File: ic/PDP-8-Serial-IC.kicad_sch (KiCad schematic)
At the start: 61 parts, among them J1 Screw_Terminal_01x06, J2 DE9_Socket_MountingHoles, J3 FlipChip_01x18, Q1 2N3904, Q2 2N3904, Q3 2N3906, U1 MAX232, U2 74HCT14, U3 L78L05_TO92

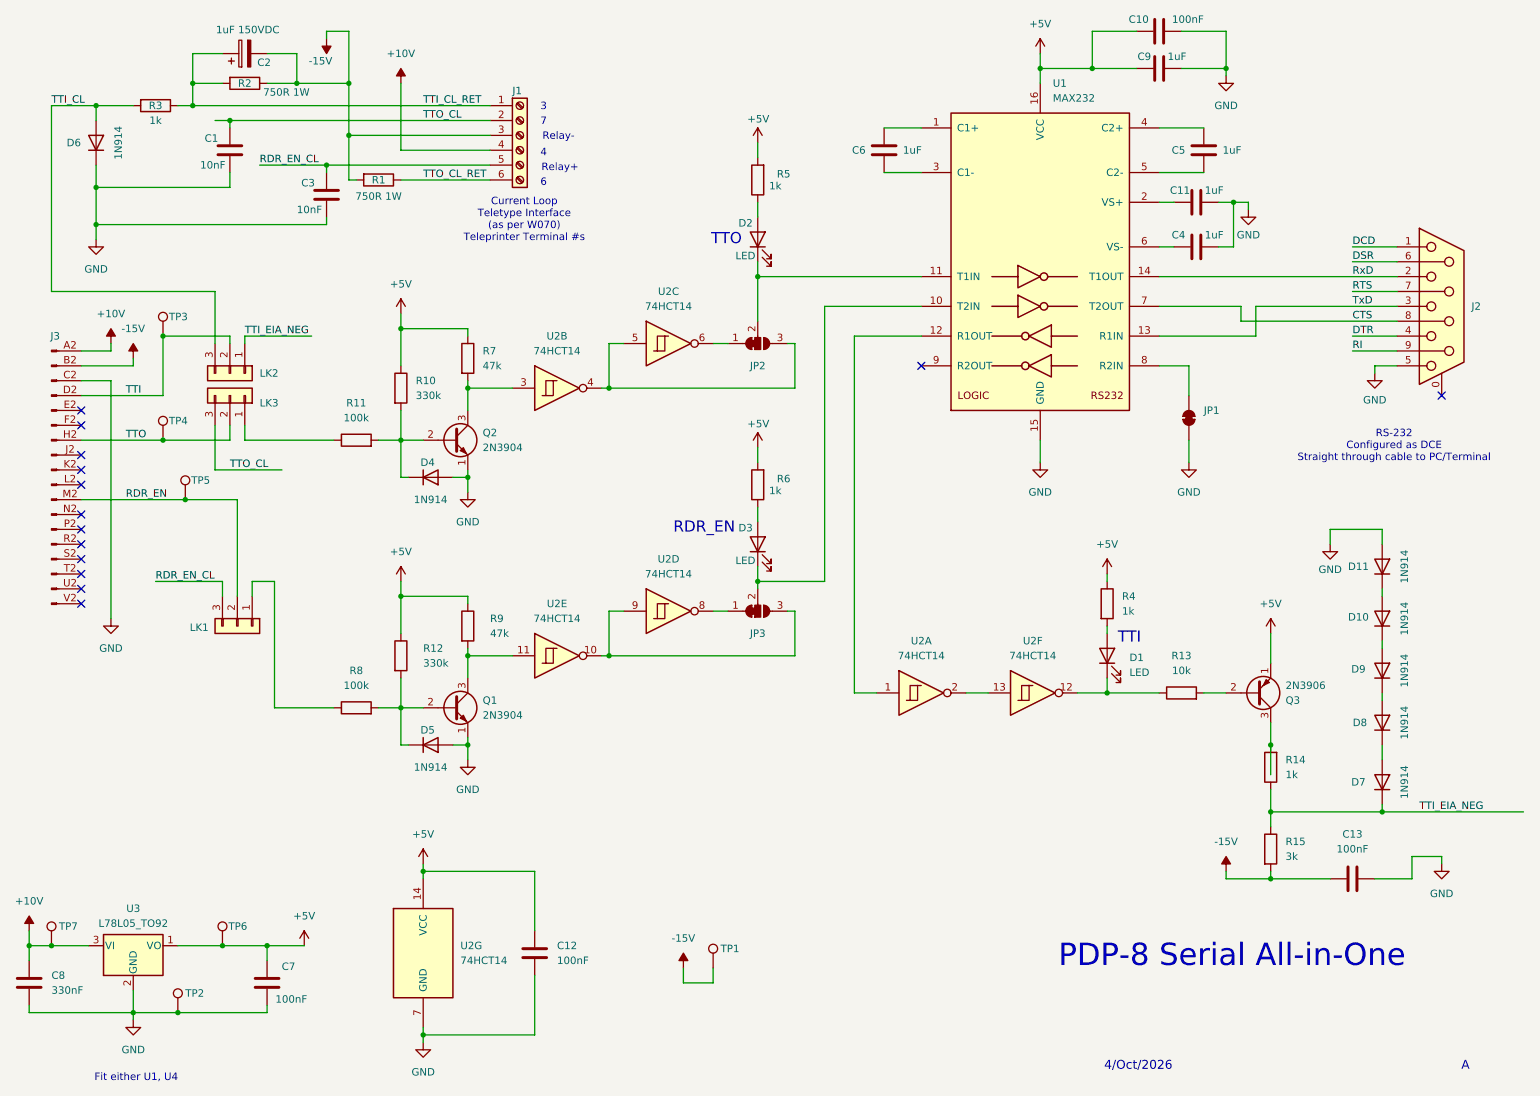
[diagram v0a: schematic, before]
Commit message: Added improved flip-chip footprint and shared lib for IC variant
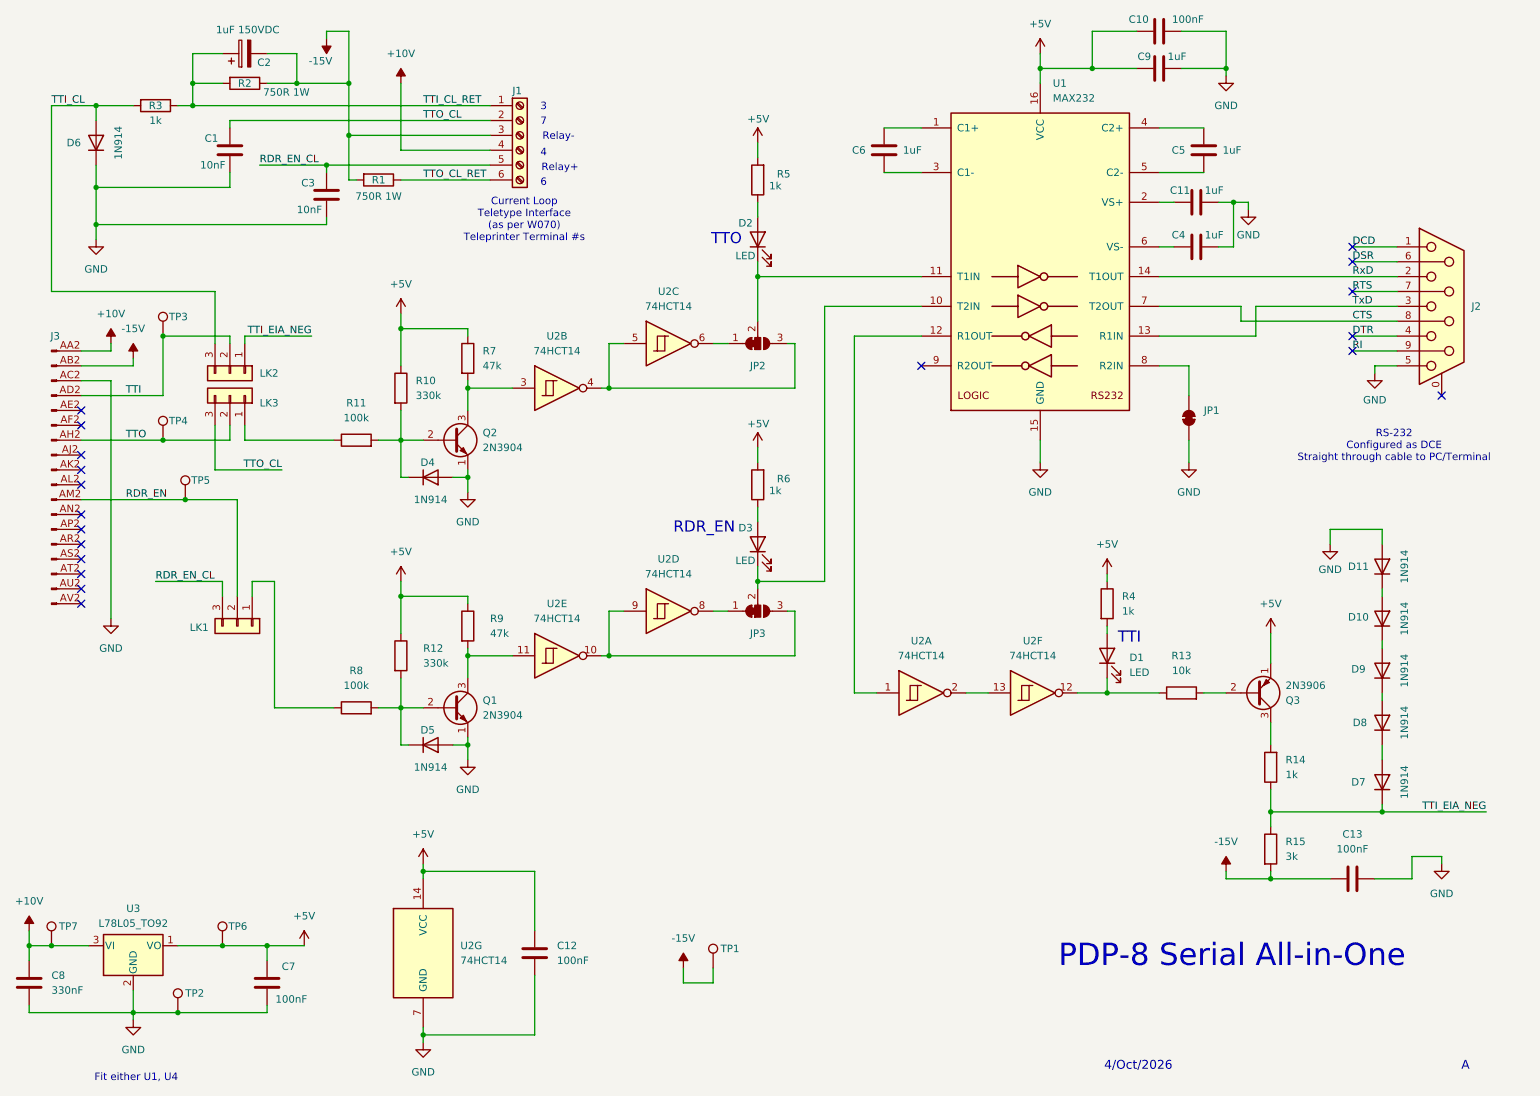
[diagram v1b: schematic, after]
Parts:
- J3: footprint DEC:FlipChip_SingleSided_CardEdge -> DEC:DEC_single_short_holeless
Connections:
- net +10V: now also J3.AA2 (Pin_A); no longer J3.A2 (Pin_A)
- net -15V: now also J3.AB2 (Pin_B); no longer J3.B2 (Pin_B)
- net GND: now also J3.AC2 (Pin_C); no longer J3.C2 (Pin_C)
- net RDR_EN: now also J3.AM2 (Pin_M); no longer J3.M2 (Pin_M)
- net TTI: now also J3.AD2 (Pin_D); no longer J3.D2 (Pin_D)
- net TTO: now also J3.AH2 (Pin_H); no longer J3.H2 (Pin_H)
- net DSR: now reaches J2.6
- no-connect marks 14 -> 19
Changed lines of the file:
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@@
 	)
 	(junction
-		(at 238.76 138.43)
-		(diameter 0)
-		(color 0 0 0 0)
-	)
-	(junction
 		(at 53.34 96.52)
 		(diameter 0)
@@
 	)
 	(junction
-		(at 60.96 31.75)
-		(diameter 0)
-		(color 0 0 0 0)
-	)
-	(junction
 		(at 38.1 29.21)
 		(diameter 0)
@@
 	)
 	(no_connect
+		(at 252.73 60.96)
+	)
+	(no_connect
+		(at 252.73 53.34)
+	)
+	(no_connect
 		(at 35.56 101.6)
 	)
 	(no_connect
+		(at 252.73 55.88)
+	)
+	(no_connect
 		(at 35.56 83.82)
 	)
@@
 		(at 35.56 109.22)
 	)
+	(no_connect
+		(at 252.73 68.58)
+	)
+	(no_connect
+		(at 252.73 71.12)
+	)
 	(wire
 		(pts
@@
 	(wire
 		(pts
-			(xy 257.81 149.86) (xy 281.94 149.86)
+			(xy 257.81 149.86) (xy 275.59 149.86)
 		)
 		(stroke
@@
 	(wire
 		(pts
-			(xy 238.76 143.51) (xy 238.76 138.43)
-		)
-		(stroke
-			(width 0)
-			(type default)
-		)
-	)
-	(wire
-		(pts
 			(xy 167.64 68.58) (xy 167.64 129.54)
 		)
@@
 	(wire
 		(pts
-			(xy 58.42 31.75) (xy 60.96 31.75)
-		)
-		(stroke
-			(width 0)
-			(type default)
-		)
-	)
-	(wire
-		(pts
 			(xy 210.82 127) (xy 210.82 129.54)
 		)
@@
 		)
 	)
-	(table
-		(column_count 2)
-		(border
-			(external yes)
-			(header yes)
-			(stroke
-				(width 0)
-				(type solid)
-			)
-		)
-		(separators
-			(rows yes)
-			(cols yes)
-			(stroke
-				(width 0)
-				(type solid)
-			)
-		)
-		(column_widths 14.478 17.526)
-		(row_heights 2.794 2.794)
-		(cells
-			(table_cell "EIA/232"
-				(exclude_from_sim no)
-				(at 46.482 53.594 0)
-				(size 14.478 2.794)
-				(margins 0.9525 0.9525 0.9525 0.9525)
-				(span 1 1)
-				(fill
-					(type none)
-				)
-				(effects
-					(font
-						(size 1.27 1.27)
-					)
-					(justify left top)
-				)
-			)
-			(table_cell "1 - 2"
-				(exclude_from_sim no)
-				(at 60.96 53.594 0)
-				(size 17.526 2.794)
-				(margins 0.9525 0.9525 0.9525 0.9525)
-				(span 1 1)
-				(fill
-					(type none)
-				)
-				(effects
-					(font
-						(size 1.27 1.27)
-					)
-					(justify left top)
-				)
-			)
-			(table_cell "Current Loop"
-				(exclude_from_sim no)
-				(at 46.482 56.388 0)
-				(size 14.478 2.794)
-				(margins 0.9525 0.9525 0.9525 0.9525)
-				(span 1 1)
-				(fill
-					(type none)
-				)
-				(effects
-					(font
-						(size 1.27 1.27)
-					)
-					(justify left top)
-				)
-			)
-			(table_cell "2 - 3"
-				(exclude_from_sim no)
-				(at 60.96 56.388 0)
-				(size 17.526 2.794)
-				(margins 0.9525 0.9525 0.9525 0.9525)
-				(span 1 1)
-				(fill
-					(type none)
-				)
-				(effects
-					(font
-						(size 1.27 1.27)
-					)
-					(justify left top)
-				)
-			)
-		)
-	)
 	(label "TTI"
 		(at 43.18 78.74 0)
@@
 	)
 	(label "TTI_EIA_NEG"
-		(at 63.5 68.58 0)
+		(at 74.93 68.58 180)
 		(effects
 			(font
 				(size 1.27 1.27)
 			)
-			(justify left bottom)
+			(justify right bottom)
 		)
 	)
@@
 	)
 	(label "TTO_CL"
-		(at 60.96 91.44 0)
+		(at 69.85 91.44 180)
 		(effects
 			(font
 				(size 1.27 1.27)
 			)
-			(justify left bottom)
+			(justify right bottom)
 		)
 	)
@@
 	)
 	(label "TTI_EIA_NEG"
-		(at 264.16 149.86 0)
+		(at 275.59 149.86 180)
 		(effects
 			(font
 				(size 1.27 1.27)
 			)
-			(justify left bottom)
+			(justify right bottom)
 		)
 	)
@@
 		)
 	)
-	(label ""
-		(at 252.73 55.88 0)
-		(effects
-			(font
-				(size 1.27 1.27)
-			)
-			(justify left bottom)
-		)
-	)
 	(symbol
 		(lib_id "Interface_UART:MAX232")
@@
 	)
 	(symbol
-		(lib_name "FlipChip_01x18_1")
-		(lib_id "DEC:FlipChip_01x18")
-		(at 30.48 91.44 0)
-		(unit 1)
-		(exclude_from_sim no)
-		(in_bom yes)
-		(on_board yes)
-		(dnp no)
-		(fields_autoplaced yes)
-		(property "Reference" "J3"
-			(at 31.115 68.58 0)
-			(effects
-				(font
-					(size 1.27 1.27)
-				)
-			)
-		)
-		(property "Value" "FlipChip_01x18"
-			(at 31.115 68.58 0)
-			(effects
-				(font
-					(size 1.27 1.27)
-				)
-				(hide yes)
-			)
-		)
-		(property "Footprint" "DEC:FlipChip_SingleSided_CardEdge"
-			(at 30.48 91.44 0)
-			(effects
-				(font
-					(size 1.27 1.27)
-				)
-				(hide yes)
-			)
-		)
-		(property "Datasheet" "~"
-			(at 30.48 91.44 0)
-			(effects
-				(font
-					(size 1.27 1.27)
-				)
-				(hide yes)
-			)
-		)
-		(property "Description" "Generic connector, single row, 01x18, script generated"
-			(at 30.48 91.44 0)
-			(effects
-				(font
-					(size 1.27 1.27)
-				)
-				(hide yes)
-			)
-		)
-		(pin "T2"
-		)
-		(pin "N2"
-		)
-		(pin "V2"
-		)
-		(pin "U2"
-		)
-		(pin "S2"
-		)
-		(pin "P2"
-		)
-		(pin "R2"
-		)
-		(pin "M2"
-		)
-		(pin "L2"
-		)
-		(pin "K2"
-		)
-		(pin "J2"
-		)
-		(pin "H2"
-		)
-		(pin "F2"
-		)
-		(pin "E2"
-		)
-		(pin "D2"
-		)
-		(pin "C2"
-		)
-		(pin "B2"
-		)
-		(pin "A2"
-		)
-		(instances
-			(project "PDP-8-Serial-IC"
-				(path "/b0fbf6eb-12c5-46d4-80aa-25b95de8bd79"
-					(reference "J3")
-					(unit 1)
-				)
-			)
-		)
-	)
-	(symbol
 		(lib_id "power:GND")
 		(at 248.92 104.14 0)
@@
 					(unit 1)
 				)
+			)
+		)
+	)
+	(symbol
+		(lib_id "DEC:FlipChip_01x18")
+		(at 30.48 91.44 0)
+		(unit 1)
+		(exclude_from_sim no)
+		(in_bom yes)
+		(on_board yes)
+		(dnp no)
+		(fields_autoplaced yes)
+		(property "Reference" "J3"
+			(at 31.115 68.58 0)
+			(effects
+				(font
+					(size 1.27 1.27)
+				)
+			)
+		)
+		(property "Value" "FlipChip_01x18"
+			(at 31.115 68.58 0)
+			(effects
+				(font
+					(size 1.27 1.27)
+				)
+				(hide yes)
+			)
+		)
+		(property "Footprint" "DEC:DEC_single_short_holeless"
+			(at 35.56 97.79 0)
+			(effects
+				(font
+					(size 1.27 1.27)
+				)
+				(hide yes)
+			)
+		)
+		(property "Datasheet" "~"
+			(at 30.48 91.44 0)
+			(effects
+				(font
+					(size 1.27 1.27)
+				)
+				(hide yes)
+			)
+		)
+		(property "Description" "Generic connector, single row, 01x18, script generated"
+			(at 34.29 101.6 0)
+			(effects
+				(font
+					(size 1.27 1.27)
+				)
+				(hide yes)
+			)
+		)
+		(pin "AR2"
+		)
+		(pin "AN2"
+		)
+		(pin "AE2"
+		)
+		(pin "AM2"
+		)
+		(pin "AJ2"
+		)
+		(pin "AL2"
+		)
+		(pin "AA2"
+		)
+		(pin "AH2"
+		)
+		(pin "AD2"
+		)
+		(pin "AF2"
+		)
+		(pin "AC2"
+		)
+		(pin "AB2"
+		)
+		(pin "AK2"
+		)
+		(pin "AU2"
+		)
+		(pin "AV2"
+		)
+		(pin "AP2"
+		)
+		(pin "AT2"
+		)
+		(pin "AS2"
+		)
+		(instances
+			(project "PDP-8-Serial-IC"
+				(path "/b0fbf6eb-12c5-46d4-80aa-25b95de8bd79"
+					(reference "J3")
+					(unit 1)
+				)
